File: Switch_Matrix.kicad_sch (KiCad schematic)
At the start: 146 parts, among them SW1 SW_Push_45deg, SW10 SW_Push_45deg, SW11 SW_Push_45deg, SW12 SW_Push_45deg, SW12(2)1 SW_Push_45deg, SW13 SW_Push_45deg, SW14 SW_Push_45deg, SW15 SW_Push_45deg, SW16 SW_Push_45deg, SW17 SW_Push_45deg, SW18 SW_Push_45deg, SW19 SW_Push_45deg, SW2 SW_Push_45deg, SW20 SW_Push_45deg, SW21 SW_Push_45deg, SW22 SW_Push_45deg, SW23 SW_Push_45deg, SW24 SW_Push_45deg, SW24(1.5)1 SW_Push_45deg, SW25 SW_Push_45deg, SW26 SW_Push_45deg, SW26(2)1 SW_Push_45deg, SW26(ISO)1 SW_Push_45deg, SW27(1.25)1 SW_Push_45deg, SW27(1.5)1 SW_Push_45deg, SW27(ortho)1 SW_Push_45deg, SW28 SW_Push_45deg, SW28(1.5stagger)1 SW_Push_45deg, SW28(ortho)1 SW_Push_45deg, SW29 SW_Push_45deg, SW29(1.5stagger)1 SW_Push_45deg, SW29(ortho)1 SW_Push_45deg, SW3 SW_Push_45deg, SW30 SW_Push_45deg, SW30(1.5stagger)1 SW_Push_45deg, SW30(ortho)1 SW_Push_45deg, SW31 SW_Push_45deg, SW31(1.5stagger)1 SW_Push_45deg, SW31(ortho)1 SW_Push_45deg, SW32 SW_Push_45deg, SW32(1.5stagger)1 SW_Push_45deg, SW32(ortho)1 SW_Push_45deg, SW33 SW_Push_45deg, SW33(1.5stagger)1 SW_Push_45deg, SW33(ortho)1 SW_Push_45deg, SW34 SW_Push_45deg, SW34(1.5stagger)1 SW_Push_45deg, SW34(ortho)1 SW_Push_45deg, SW35 SW_Push_45deg, SW35(1.5stagger)1 SW_Push_45deg, SW35(ortho)1 SW_Push_45deg, SW36 SW_Push_45deg, SW36(1.5stagger)1 SW_Push_45deg, SW36(ortho)1 SW_Push_45deg, SW37 SW_Push_45deg, SW37(1.5stagger)1 SW_Push_45deg, SW37(ortho)1 SW_Push_45deg, SW38(1.25)1 SW_Push_45deg, SW38(1.5)1 SW_Push_45deg, SW38(ortho)1 SW_Push_45deg, SW39 SW_Push_45deg, SW39(1.5)1 SW_Push_45deg, SW4 SW_Push_45deg, SW40 SW_Push_45deg, SW40(3)1 SW_Push_45deg, SW41 SW_Push_45deg, SW41(1.5)1 SW_Push_45deg, SW42(1.25)1 SW_Push_45deg, SW42(1.5)1 SW_Push_45deg, SW42(3)1 SW_Push_45deg, SW43(1.75)1 SW_Push_45deg, SW43(2)1 SW_Push_45deg, SW44(3)1 SW_Push_45deg, SW44(4)1 SW_Push_45deg, SW44(6)1 SW_Push_45deg, SW45(1.75)1 SW_Push_45deg, SW45(2)1 SW_Push_45deg, SW46(1.25)1 SW_Push_45deg, SW46(1.5)1 SW_Push_45deg, SW46(3)1 SW_Push_45deg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

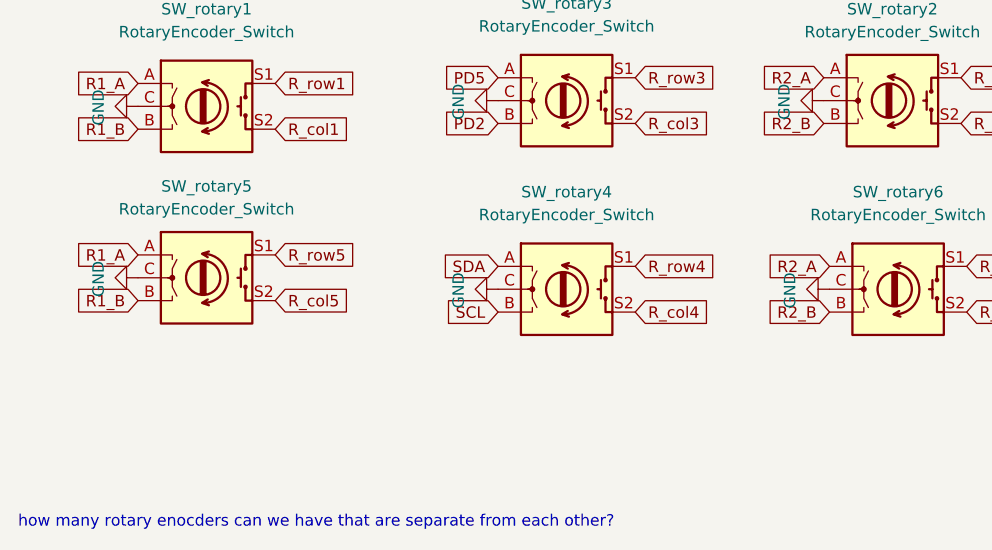
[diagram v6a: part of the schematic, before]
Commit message: rgb fixed, rotaries separately reconnected
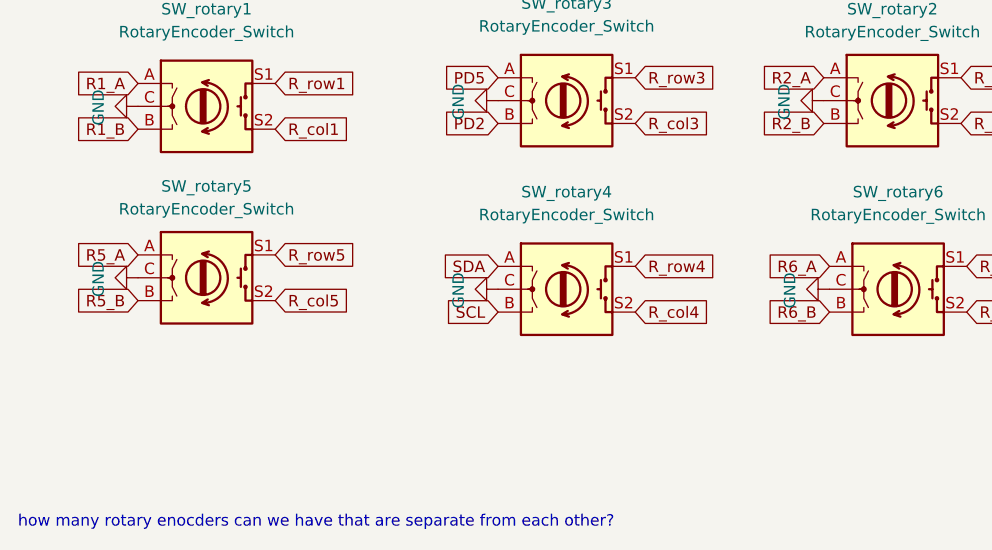
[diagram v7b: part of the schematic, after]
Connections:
- net R1_A: no longer SW_rotary5.A
- net R1_B: no longer SW_rotary5.B
- net R2_A: no longer SW_rotary6.A
- net R2_B: no longer SW_rotary6.B
- new net R5_A: SW_rotary5.A
- new net R5_B: SW_rotary5.B
- new net R6_A: SW_rotary6.A
- new net R6_B: SW_rotary6.B
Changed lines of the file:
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@@
     (effects (font (size 1.27 1.27)) (justify left bottom))
   )
-  (global_label "R2_A" (shape input) (at 115.57 163.195 180) (fields_autoplaced)
+  (global_label "R6_A" (shape input) (at 115.57 163.195 180) (fields_autoplaced)
     (effects (font (size 1.27 1.27)) (justify right))
     (property "Intersheet References" "${INTERSHEET_REFS}" (id 0) (at 108.6212 163.1156 0)
@@
     )
   )
-  (global_label "R2_B" (shape input) (at 115.57 168.275 180) (fields_autoplaced)
+  (global_label "R6_B" (shape input) (at 115.57 168.275 180) (fields_autoplaced)
     (effects (font (size 1.27 1.27)) (justify right))
     (property "Intersheet References" "${INTERSHEET_REFS}" (id 0) (at 108.4398 168.1956 0)
@@
     )
   )
-  (global_label "R1_A" (shape input) (at 38.735 161.925 180) (fields_autoplaced)
+  (global_label "R5_A" (shape input) (at 38.735 161.925 180) (fields_autoplaced)
     (effects (font (size 1.27 1.27)) (justify right))
     (property "Intersheet References" "${INTERSHEET_REFS}" (id 0) (at 31.7862 161.8456 0)
@@
     )
   )
-  (global_label "R1_B" (shape input) (at 38.735 167.005 180) (fields_autoplaced)
+  (global_label "R5_B" (shape input) (at 38.735 167.005 180) (fields_autoplaced)
     (effects (font (size 1.27 1.27)) (justify right))
     (property "Intersheet References" "${INTERSHEET_REFS}" (id 0) (at 31.6048 166.9256 0)

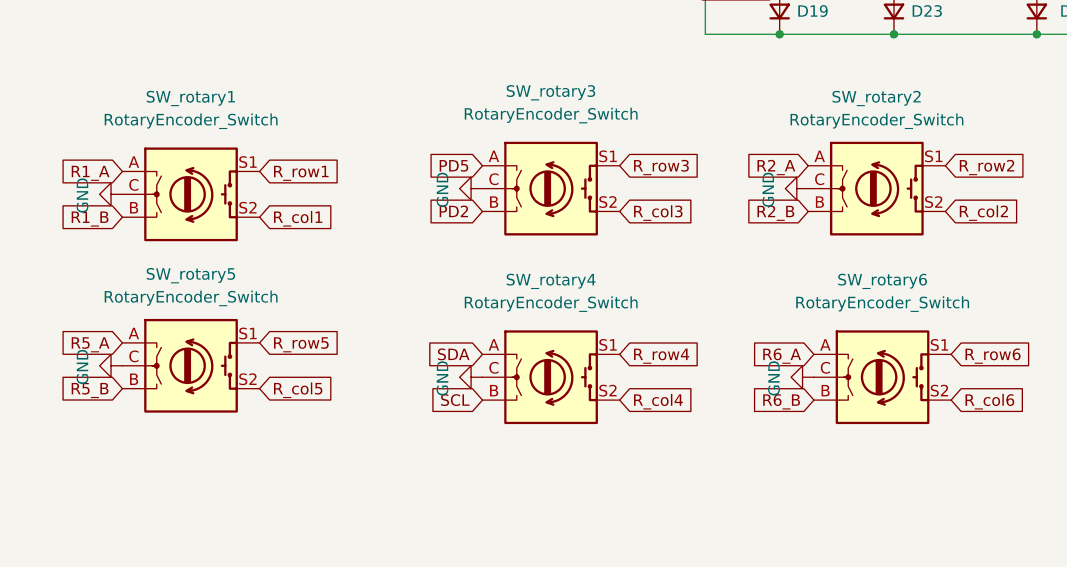
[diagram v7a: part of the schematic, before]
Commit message: finished new PCB draft
ran preliminary DRC
cleaned up project folder
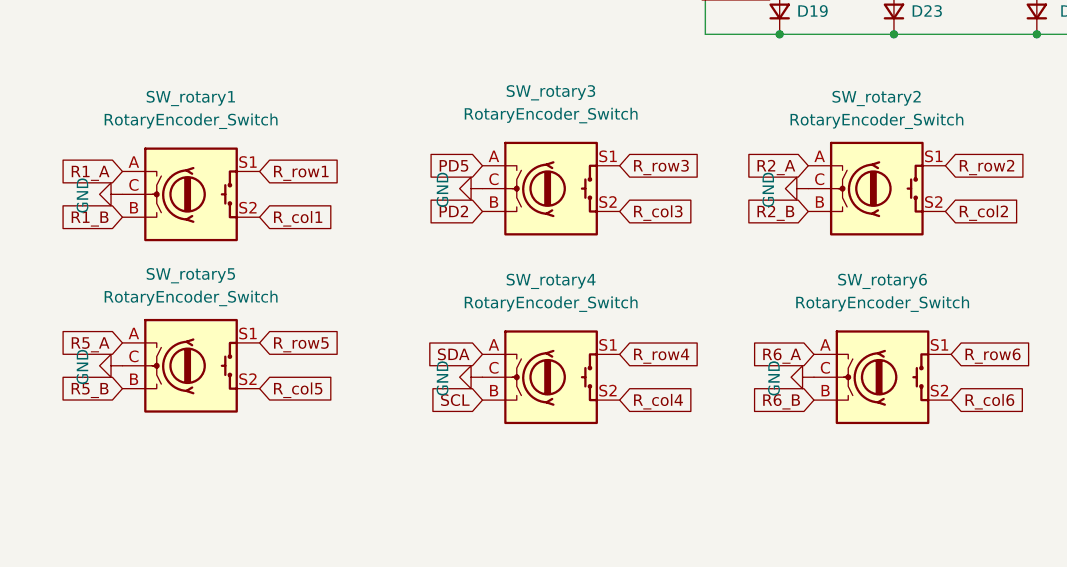
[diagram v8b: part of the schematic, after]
